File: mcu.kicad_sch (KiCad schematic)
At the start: 47 parts, among them U1 STM32U5G9ZJTxQ, Y1 NX2016SA-16MHZ-EXS00A-CS07826, Y2 NX2012SA-32.768K-STD-MUB-1

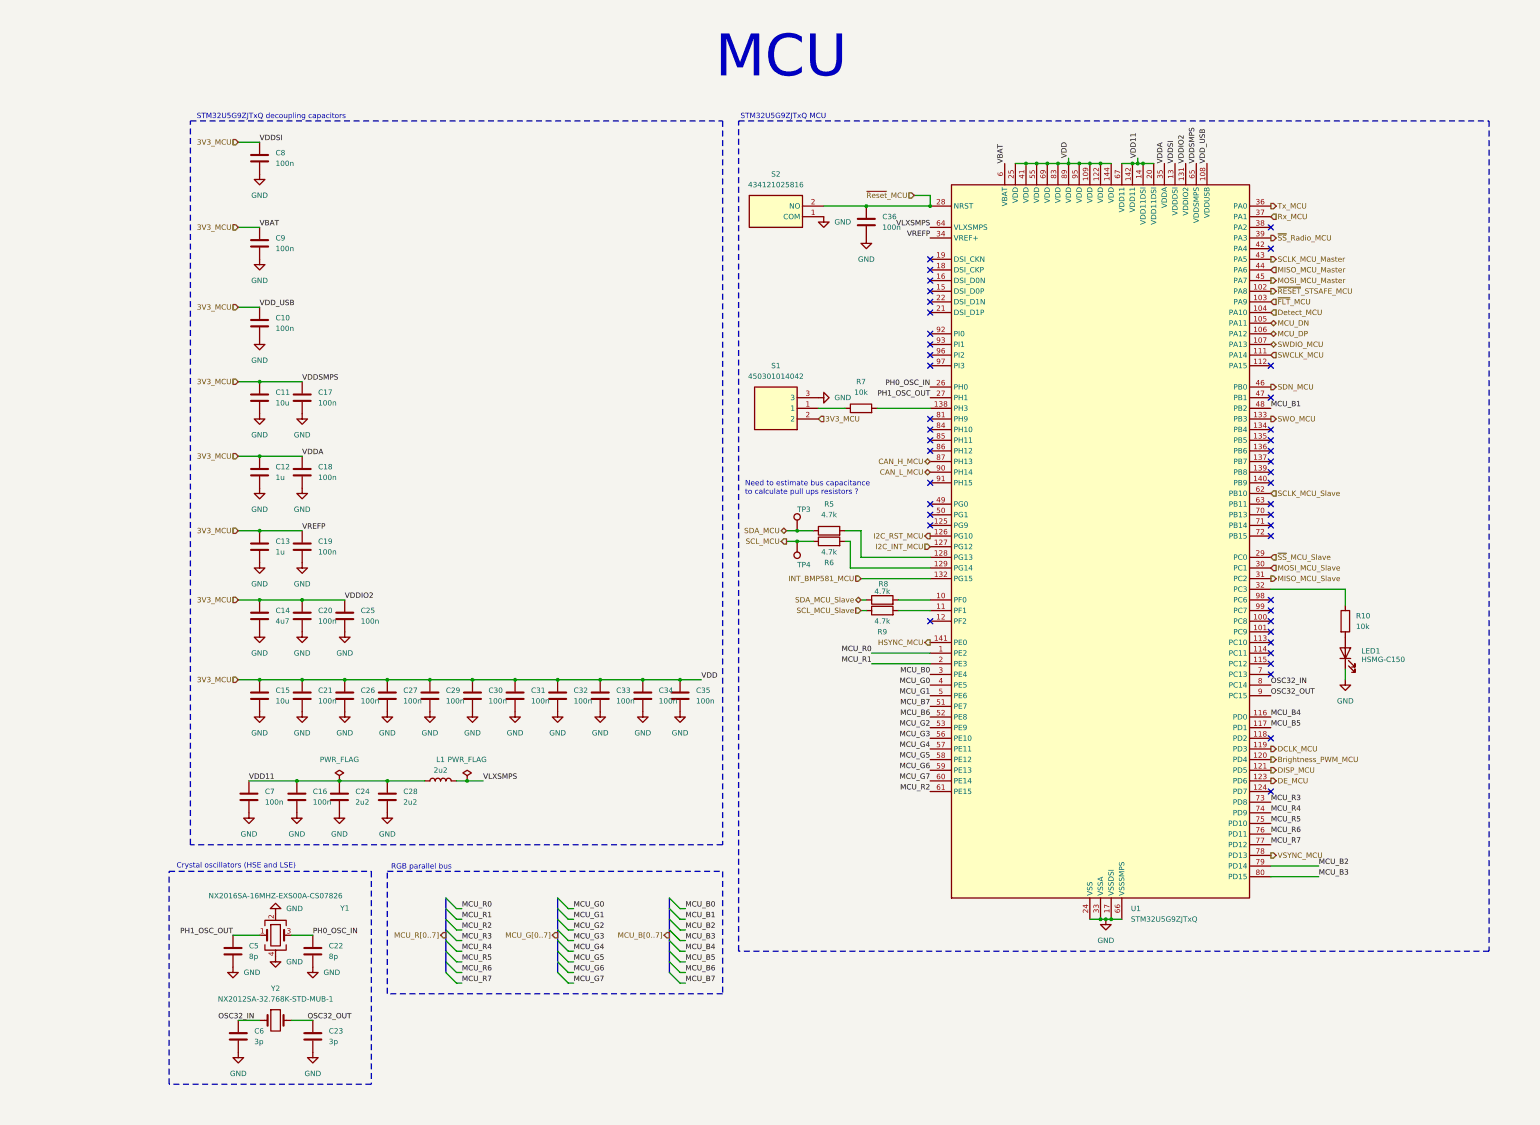
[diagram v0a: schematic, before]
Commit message: Fiw warnings concerning multiple name for the same label
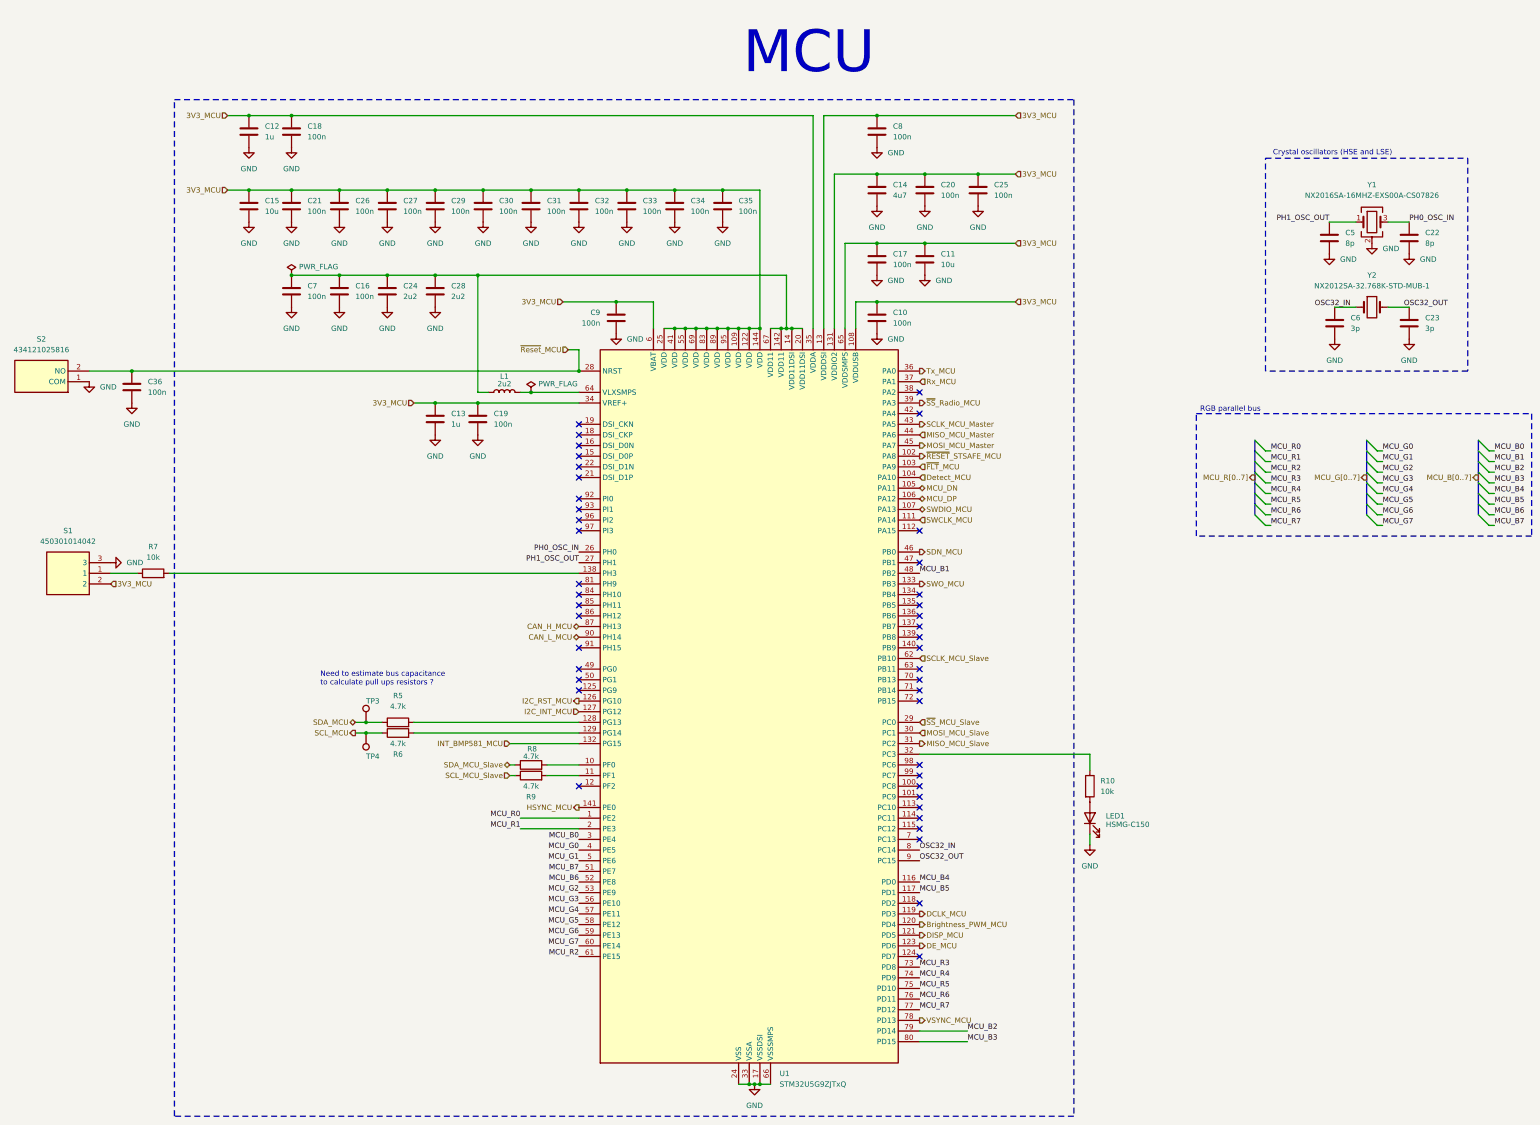
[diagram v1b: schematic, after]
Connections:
- net 3V3_MCU: now also C17.2, C8.2, C9.2; no longer C17.1, C8.1, C9.1
- net GND: now also C17.1, C8.1, C9.1; no longer C17.2, C8.2, C9.2
- net VDD11: no longer names the net of C16.1, C24.1, C28.1, C7.1, U1.14 (VDD11DSI), U1.142 (VDD11), U1.20 (VDD11DSI), U1.67 (VDD11)
- net VDD11: now also L1.2; no longer L1.1
- net VLXSMPS: no longer names the net of U1.64 (VLXSMPS)
- net VLXSMPS: now also L1.1; no longer L1.2
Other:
- note removed: "STM32U5G9ZJTxQ MCU"
- note removed: "STM32U5G9ZJTxQ decoupling capacitors"
- moved on the sheet: C10, C11, C12, C13, C14, C15, C16, C17, C18, C19, C20, C21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
